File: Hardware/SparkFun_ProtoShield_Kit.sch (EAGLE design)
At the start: 29 parts

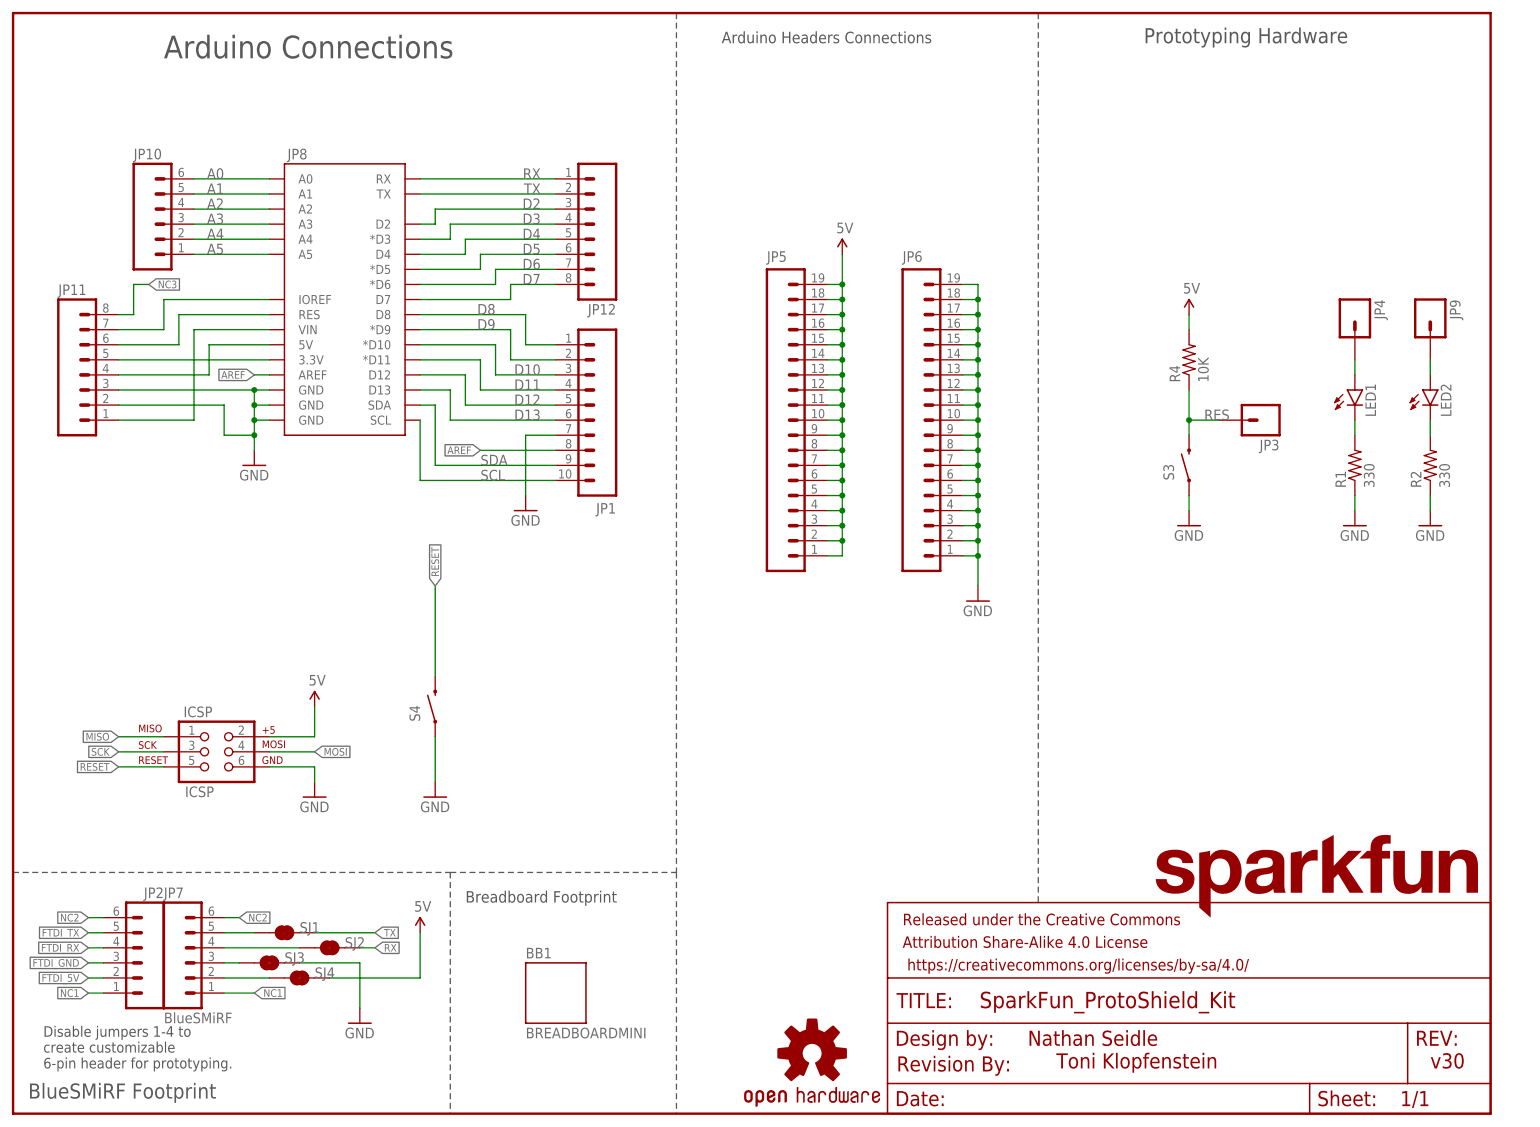
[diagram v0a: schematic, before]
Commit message: Add files via upload
-updated labels and silkscreen
-changed names to vectors
-flipped the BlueSMiRF header's orientation so that the bluetooth faces out away from the board
-modified traces for the BlueSMiRF
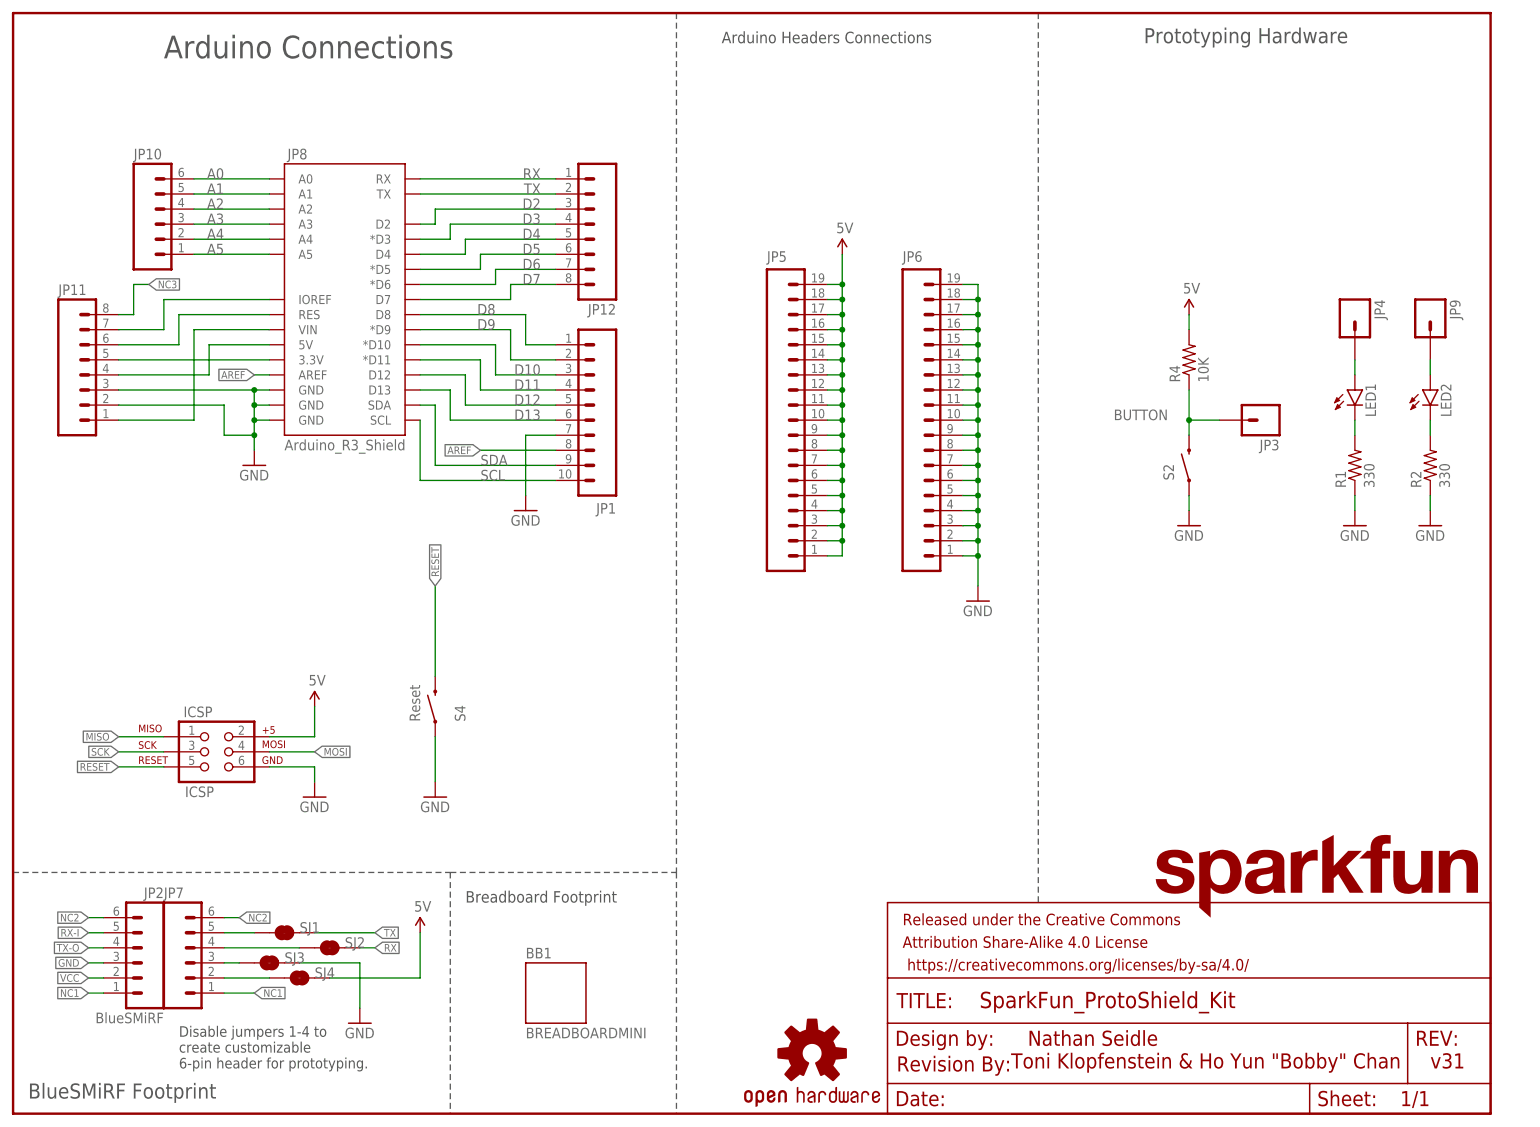
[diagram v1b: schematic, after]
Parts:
- JP2: value (none) -> BlueSMiRF
- JP7: value BlueSMiRF -> (none)
- renumbered S3 to S2
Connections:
- net FTDI_5V renamed VCC
- net FTDI_RX renamed TX-O
- net FTDI_TX renamed RX-I
- net RES renamed BUTTON
- removed net FTDI_GND: JP2.3, JP7.3, SJ3.1
- net GND: now also JP2.3, JP7.3, SJ3.1
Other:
- note added: "Arduino_R3_Shield"
- note added: "Reset"
- note added: "Toni Klopfenstein & Ho Yun "Bobby" Chan"
- note added: "v31"
- note removed: "Toni Klopfenstein"
- note removed: "v30"
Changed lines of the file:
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@@
 <?xml version="1.0" encoding="utf-8"?>
 <!DOCTYPE eagle SYSTEM "eagle.dtd">
-<eagle version="7.5.0">
+<eagle version="7.7.0">
 <drawing>
 <settings>
@@
 <part name="JP3" library="SparkFun-Connectors" deviceset="M01" device="PTH"/>
 <part name="U$1" library="SparkFun-Aesthetics" deviceset="SFE_LOGO_NAME" device=".1_INCH"/>
-<part name="JP7" library="SparkFun-Connectors" deviceset="M06" device="SILK_FEMALE_PTH" value="BlueSMiRF"/>
+<part name="JP7" library="SparkFun-Connectors" deviceset="M06" device="SILK_FEMALE_PTH"/>
 <part name="P+1" library="SparkFun-Aesthetics" deviceset="5V" device="" value="5V"/>
 <part name="U$2" library="SparkFun-Aesthetics" deviceset="REVISION" device=""/>
@@
 <part name="JP11" library="SparkFun-Connectors" deviceset="M08" device=""/>
 <part name="JP1" library="SparkFun-Connectors" deviceset="M10" device="SILK_FEMALE_PTH"/>
-<part name="S3" library="SparkFun-Electromechanical" deviceset="SWITCH-MOMENTARY-2" device="PTH"/>
+<part name="S2" library="SparkFun-Electromechanical" deviceset="SWITCH-MOMENTARY-2" device="PTH"/>
 <part name="S4" library="SparkFun-Electromechanical" deviceset="SWITCH-MOMENTARY-2" device="PTH"/>
 <part name="GND8" library="SparkFun-Aesthetics" deviceset="GND" device=""/>
@@
 <part name="SJ4" library="SparkFun-Passives" deviceset="JUMPER-PAD-2-NC_BY_TRACE" device=""/>
 <part name="LOGO1" library="SparkFun-Aesthetics" deviceset="OSHW-LOGO" device="S"/>
-<part name="JP2" library="SparkFun-Connectors" deviceset="M06" device="SILK_FEMALE_PTH"/>
+<part name="JP2" library="SparkFun-Connectors" deviceset="M06" device="SILK_FEMALE_PTH" value="BlueSMiRF"/>
 <part name="P+3" library="SparkFun-Aesthetics" deviceset="5V" device="" value="5V"/>
 <part name="GND6" library="SparkFun-Aesthetics" deviceset="GND" device=""/>
@@
 <plain>
 <text x="170.942" y="11.43" size="2.54" layer="94">Nathan Seidle</text>
-<text x="238.76" y="7.62" size="2.54" layer="94">v30</text>
-<text x="175.768" y="7.62" size="2.54" layer="94">Toni Klopfenstein</text>
+<text x="238.76" y="7.62" size="2.54" layer="94">v31</text>
+<text x="168.148" y="7.62" size="2.54" layer="94">Toni Klopfenstein &amp; Ho Yun "Bobby" Chan</text>
 <wire x1="0" y1="40.64" x2="73.66" y2="40.64" width="0.1524" layer="97" style="longdash"/>
 <wire x1="73.66" y1="40.64" x2="73.66" y2="0" width="0.1524" layer="97" style="longdash"/>
@@
 <text x="76.2" y="35.56" size="1.9304" layer="97">Breadboard Footprint</text>
 <text x="2.54" y="2.54" size="2.54" layer="97">BlueSMiRF Footprint</text>
-<text x="5.08" y="7.62" size="1.778" layer="97">Disable jumpers 1-4 to
+<text x="27.94" y="7.62" size="1.778" layer="97">Disable jumpers 1-4 to
 create customizable
 6-pin header for prototyping.</text>
+<text x="45.72" y="111.76" size="1.778" layer="95">Arduino_R3_Shield</text>
+<text x="68.58" y="66.04" size="1.778" layer="95" rot="R90">Reset</text>
 </plain>
 <instances>
@@
 <instance part="JP11" gate="G$1" x="12.7" y="124.46"/>
 <instance part="JP1" gate="G$1" x="101.6" y="111.76" rot="R180"/>
-<instance part="S3" gate="G$1" x="198.12" y="109.22" smashed="yes" rot="R90">
+<instance part="S2" gate="G$1" x="198.12" y="109.22" smashed="yes" rot="R90">
 <attribute name="NAME" x="195.58" y="106.68" size="1.778" layer="95" rot="R90"/>
 </instance>
 <instance part="S4" gate="G$1" x="71.12" y="68.58" smashed="yes" rot="R90">
-<attribute name="NAME" x="68.58" y="66.04" size="1.778" layer="95" rot="R90"/>
+<attribute name="NAME" x="76.2" y="66.04" size="1.778" layer="95" rot="R90"/>
 </instance>
 <instance part="GND8" gate="1" x="40.64" y="109.22"/>
@@
 <wire x1="198.12" y1="104.14" x2="198.12" y2="101.6" width="0.1524" layer="91"/>
 <pinref part="GND5" gate="1" pin="GND"/>
-<pinref part="S3" gate="G$1" pin="1"/>
+<pinref part="S2" gate="G$1" pin="1"/>
 </segment>
 <segment>
@@
 <pinref part="GND6" gate="1" pin="GND"/>
 <wire x1="58.42" y1="25.4" x2="58.42" y2="17.78" width="0.1524" layer="91"/>
+</segment>
+<segment>
+<pinref part="JP2" gate="G$1" pin="3"/>
+<wire x1="15.24" y1="25.4" x2="12.7" y2="25.4" width="0.1524" layer="91"/>
+<label x="12.7" y="25.4" size="1.27" layer="95" rot="R180" xref="yes"/>
+</segment>
+<segment>
+<pinref part="JP7" gate="G$1" pin="3"/>
+<pinref part="SJ3" gate="G$1" pin="1"/>
+<wire x1="35.56" y1="25.4" x2="38.1" y2="25.4" width="0.1524" layer="91"/>
 </segment>
 </net>
@@
 </segment>
 </net>
-<net name="RES" class="0">
+<net name="BUTTON" class="0">
 <segment>
 <wire x1="198.12" y1="114.3" x2="198.12" y2="116.84" width="0.1524" layer="91"/>
-<label x="200.66" y="116.84" size="1.778" layer="95"/>
+<label x="185.42" y="116.84" size="1.778" layer="95"/>
 <pinref part="R4" gate="G$1" pin="1"/>
-<pinref part="S3" gate="G$1" pin="2"/>
+<pinref part="S2" gate="G$1" pin="2"/>
 <pinref part="JP3" gate="G$1" pin="1"/>
 <wire x1="198.12" y1="116.84" x2="198.12" y2="121.92" width="0.1524" layer="91"/>
@@
 </segment>
 </net>
-<net name="FTDI_TX" class="0">
+<net name="RX-I" class="0">
 <segment>
 <pinref part="JP7" gate="G$1" pin="5"/>
@@
 </segment>
 </net>
-<net name="FTDI_RX" class="0">
+<net name="TX-O" class="0">
 <segment>
 <pinref part="JP7" gate="G$1" pin="4"/>
@@
 </segment>
 </net>
-<net name="FTDI_GND" class="0">
-<segment>
-<pinref part="JP7" gate="G$1" pin="3"/>
-<pinref part="SJ3" gate="G$1" pin="1"/>
-<wire x1="35.56" y1="25.4" x2="38.1" y2="25.4" width="0.1524" layer="91"/>
-</segment>
-<segment>
-<pinref part="JP2" gate="G$1" pin="3"/>
-<wire x1="15.24" y1="25.4" x2="12.7" y2="25.4" width="0.1524" layer="91"/>
-<label x="12.7" y="25.4" size="1.27" layer="95" rot="R180" xref="yes"/>
-</segment>
-</net>
-<net name="FTDI_5V" class="0">
+<net name="VCC" class="0">
 <segment>
 <pinref part="JP2" gate="G$1" pin="2"/>

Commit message: Update files
**Board**

* Align the 5V/GND silk screen.
* Replace the SparkFun logo with a SparkFun logo w/flame, in the SparkFun Aesthetics library.
* Add the silk for the Arduino PTH headers on the bottom side as well. 
* Fix placement and size of the BlueSMiRF text on the underside of the shield. 
* Add silkscreen for the UART pins for BlueSMiRF.
* Add copper boundary around GND trace so that it can be easily cut.
* Adjust position of prototyping hardware header.

**Schematic**

* Change all text to “vector”.
* Change the labels for the various boxes so they are the same ratio and size. 
* Change all dashed lines to “Short Dash”.
* Update all outdated packages to our current Sparkfun Library packages (i.e. GND symbols are not current, 5V arrow, Switches, etc. ).
* Place the Open Hardware symbol next to the SparkFun symbol. 
* Net the GND net flag on the BlueSMiRF header to a GND symbol. 
* Update the wires on the ISCP header to indicate that the MISO and MOSI lines are not connected to anything on the proto (i.e.“MOSI NC” flag).
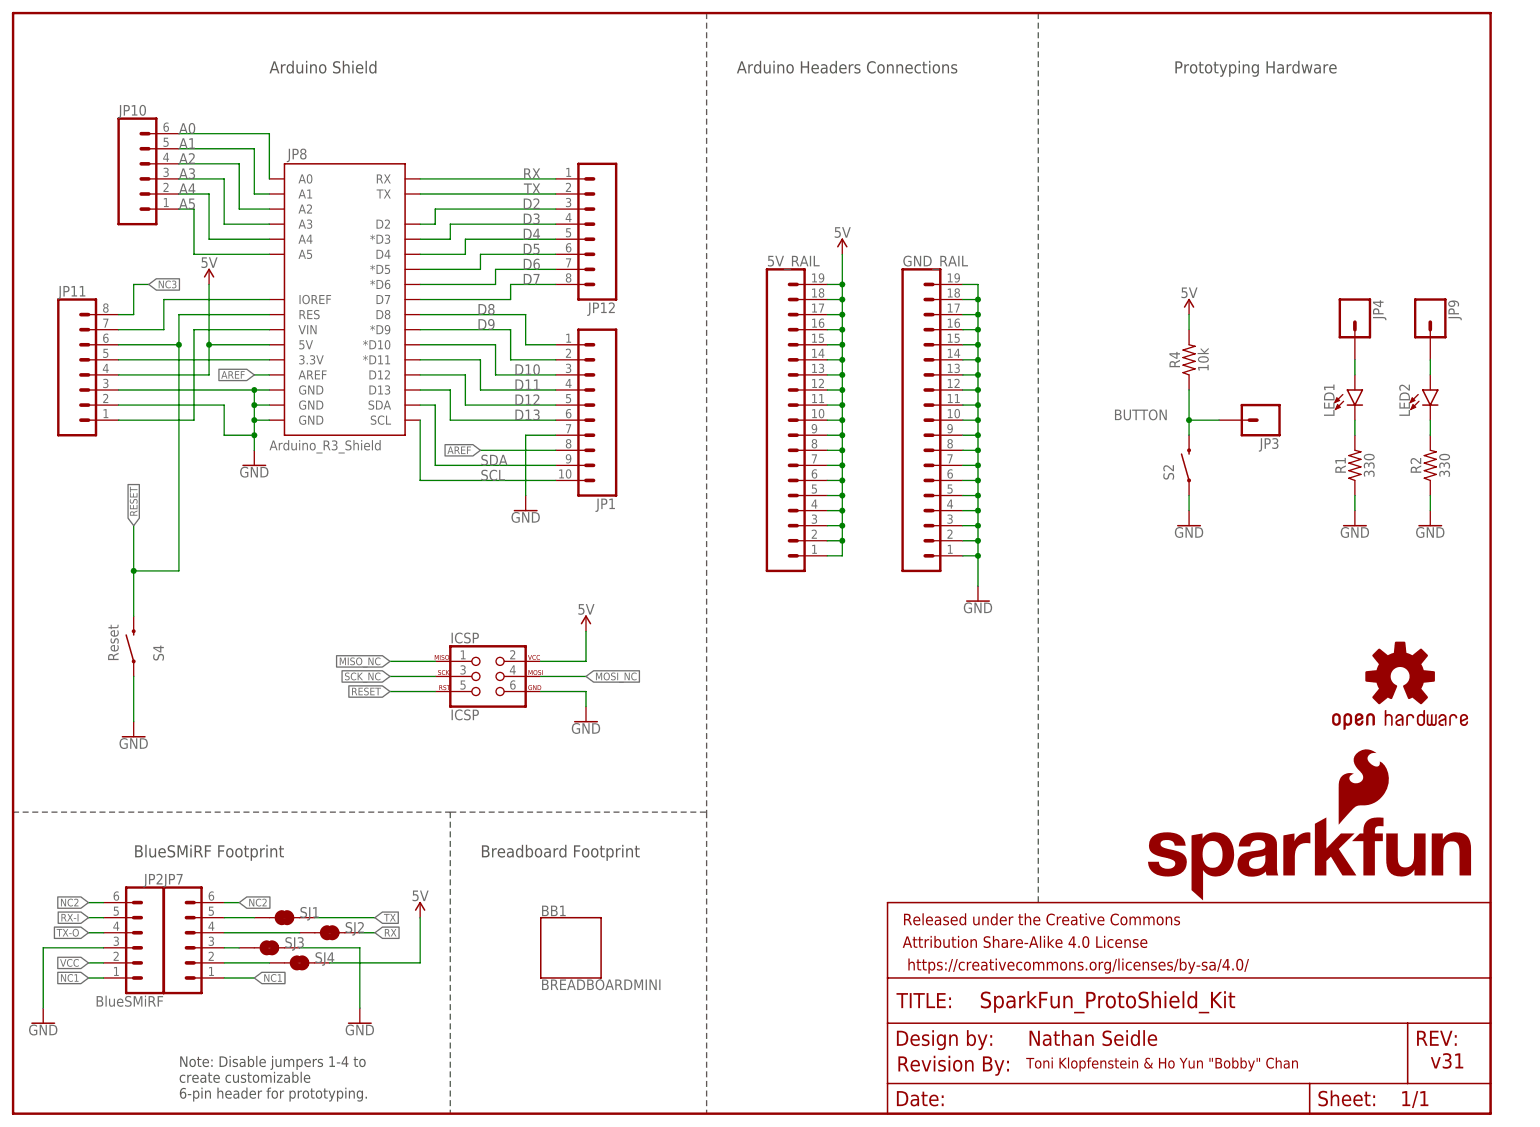
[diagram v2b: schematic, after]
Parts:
- removed JP5, JP6: (no value), SparkFun-Connectors:M191X19
- added 5V_RAIL, GND_RAIL: (no value), SparkFun-Connectors:CONN_19
- ICSP: device SparkFun-Connectors:AVR_SPI_PRG_6PTH -> SparkFun-Connectors:AVR_SPI_PROG_3X2PTH
- JP1: device SparkFun-Connectors:M10SILK_FEMALE_PTH -> SparkFun-Connectors:CONN_10"
- JP10, JP2, JP7: device SparkFun-Connectors:M06SILK_FEMALE_PTH -> SparkFun-Connectors:CONN_06SILK_FEMALE_PTH
- JP11, JP12: device SparkFun-Connectors:M08 -> SparkFun-Connectors:CONN_08"
- JP3, JP4, JP9: device SparkFun-Connectors:M01PTH -> SparkFun-Connectors:CONN_01
- R1, R2: device SparkFun-Resistors:RESISTORAXIAL-0.3 -> SparkFun-Resistors:330OHM-HORIZ-1/10W-5%
- R4: value 10K -> 10k; device SparkFun-Resistors:RESISTORAXIAL-0.3 -> SparkFun-Resistors:10KOHM-HORIZ-1/4W-5%
- S2, S4: value SWITCH-MOMENTARY-2PTH -> MOMENTARY-SWITCH-SPST-PTH-6.0MM-KIT; device SparkFun-Electromechanical:SWITCH-MOMENTARY-2PTH -> SparkFun-Switches:MOMENTARY-SWITCH-SPST-PTH-6.0MM-KIT
- SJ1, SJ2, SJ3, SJ4: value JUMPER-PAD-2-NC_BY_TRACE -> JUMPER-SMT_2_NC_TRACE_SILK; device SparkFun-Passives:JUMPER-PAD-2-NC_BY_TRACE -> SparkFun-Jumpers:JUMPER-SMT_2_NC_TRACE_SILK
- U$1: value SFE_LOGO_NAME.1_INCH -> SFE_LOGO_NAME_FLAME.1_INCH; device SparkFun-Aesthetics:SFE_LOGO_NAME.1_INCH -> SparkFun-Aesthetics:SFE_LOGO_NAME_FLAME.1_INCH
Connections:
- net MISO renamed MISO_NC
- net MOSI renamed MOSI_NC
- net N$185 renamed VIN
- net N$8 renamed 3.3
- net SCK renamed SCK_NC
- net 5V: now also 5V_RAIL.1, 5V_RAIL.10, 5V_RAIL.11, 5V_RAIL.12, 5V_RAIL.13, 5V_RAIL.14, 5V_RAIL.15, 5V_RAIL.16, 5V_RAIL.17, 5V_RAIL.18, 5V_RAIL.19, 5V_RAIL.2, 5V_RAIL.3, 5V_RAIL.4, 5V_RAIL.5, 5V_RAIL.6, 5V_RAIL.7, 5V_RAIL.8, 5V_RAIL.9; no longer JP5.1, JP5.10, JP5.11, JP5.12, JP5.13, JP5.14, JP5.15, JP5.16, JP5.17, JP5.18, JP5.19, JP5.2, JP5.3, JP5.4, JP5.5, JP5.6, JP5.7, JP5.8, JP5.9
- net GND: now also GND_RAIL.1, GND_RAIL.10, GND_RAIL.11, GND_RAIL.12, GND_RAIL.13, GND_RAIL.14, GND_RAIL.15, GND_RAIL.16, GND_RAIL.17, GND_RAIL.18, GND_RAIL.19, GND_RAIL.2, GND_RAIL.3, GND_RAIL.4, GND_RAIL.5, GND_RAIL.6, GND_RAIL.7, GND_RAIL.8, GND_RAIL.9; no longer JP6.1, JP6.10, JP6.11, JP6.12, JP6.13, JP6.14, JP6.15, JP6.16, JP6.17, JP6.18, JP6.19, JP6.2, JP6.3, JP6.4, JP6.5, JP6.6, JP6.7, JP6.8, JP6.9
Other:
- note added: "A0"
- note added: "A1"
- note added: "A2"
- note added: "A3"
- note added: "A4"
- note added: "A5"
- note added: "Arduino Shield"
- note added: "Note: Disable jumpers 1-4 to create customizable 6-pin header for prototyping."
- note removed: "Arduino Connections"
- note removed: "Disable jumpers 1-4 to create customizable 6-pin header for prototyping."
- moved on the sheet: BB1, ICSP, JP10, JP2, JP7, S4, SJ1, SJ2, SJ3, SJ4
